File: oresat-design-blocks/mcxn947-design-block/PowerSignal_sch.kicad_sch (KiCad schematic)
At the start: 64 parts, among them J1 BKUP-BATT, J3 CAN, J4 TERM, J5 10pin ARM SWD, J6 FTDI-UART-6PIN, SW1 RESET, SW2 ISP(BOOT), U1 MCXN947VKLT, U2 TCAN330, U3 TPS62111RSA, Y1 24 MHz, Y2 32.768 KHz

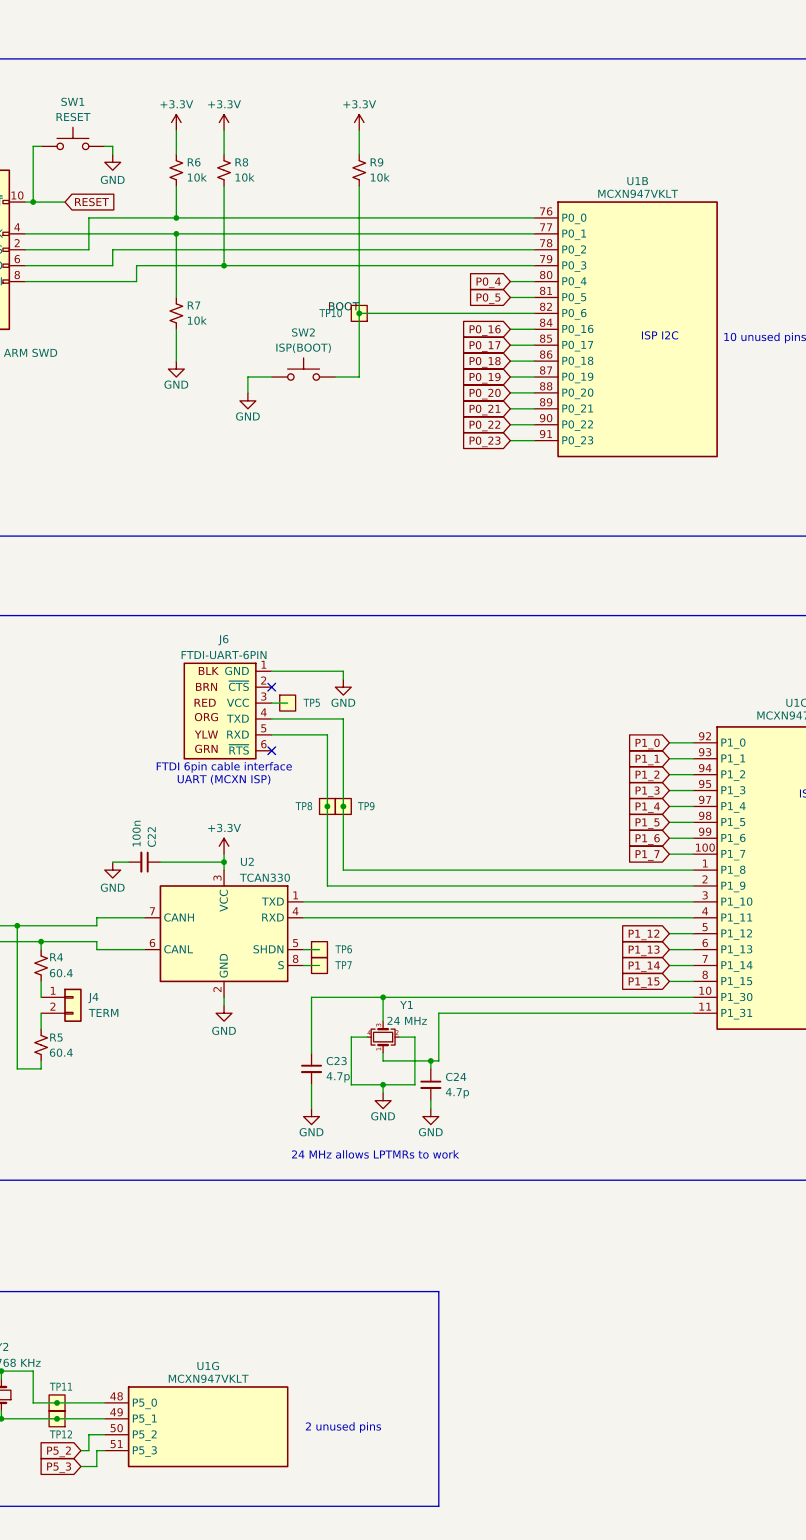
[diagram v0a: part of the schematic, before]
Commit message: finished initial layout and routing
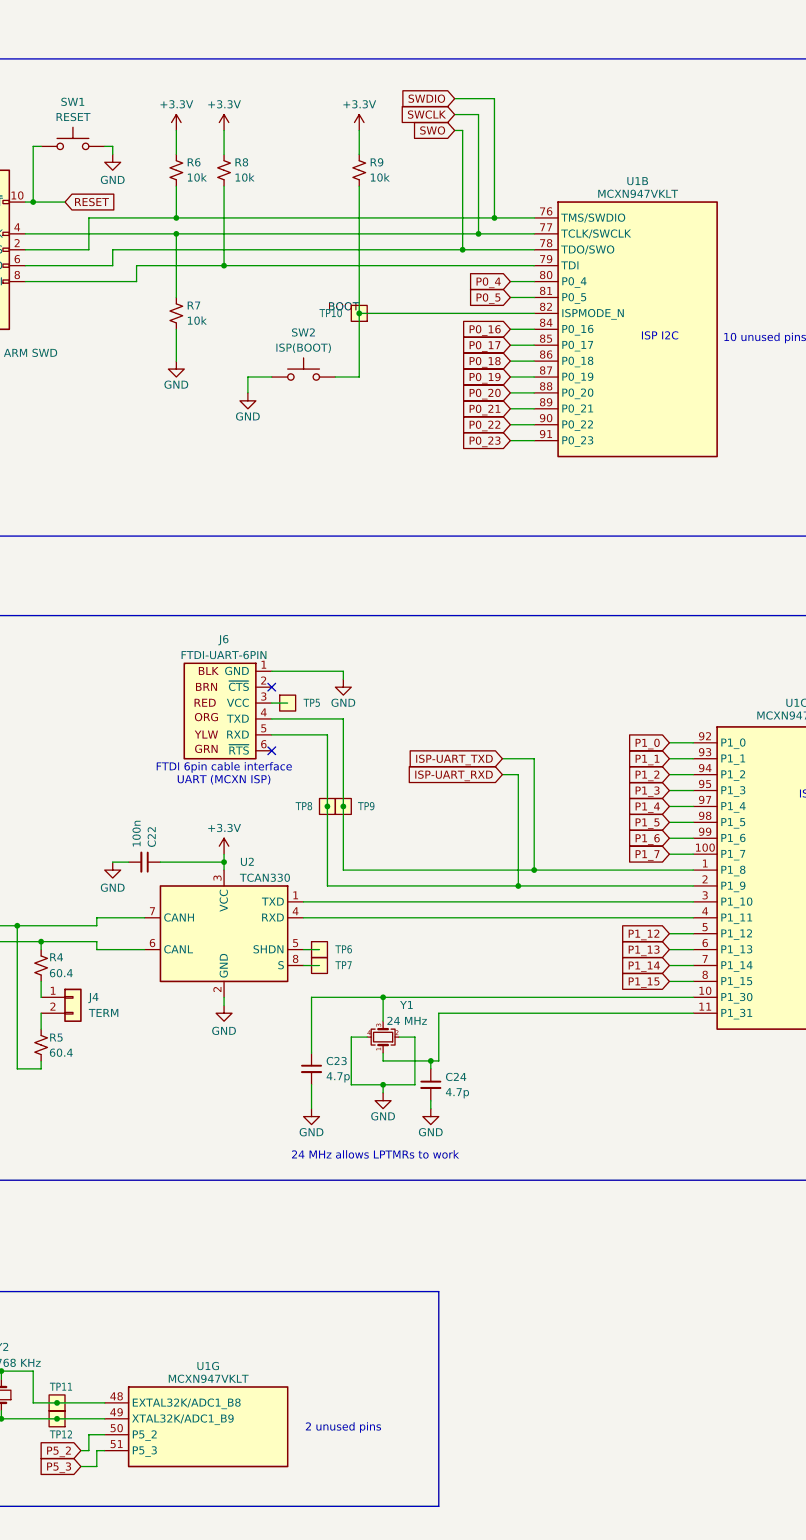
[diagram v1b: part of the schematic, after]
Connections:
- net ISP-UART_TXD: now reaches J6.4 (TXD), TP9.1, U1.1 (P1_8)
- net ISP-UART_RXD: now reaches J6.5 (RXD), TP8.1, U1.2 (P1_9)
- net SWDIO: now reaches J5.2 (SWDIO/TMS), R6.1, U1.76 (P0_0)
- net SWCLK: now reaches J5.4 (SWCLK/TCK), R7.2, U1.77 (P0_1)
- net SWO: now reaches J5.6 (SWO/TDO), U1.78 (P0_2)

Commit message: Some ERC checking and fixing, and then dep dive into oresat passive library. Sorry Anna. Go fix all the silkscreen.
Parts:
- C10, C11, C12, C13, C14, C15, C16, C2, C20, C22, C23, C24, C25, C26, C3, C4, C6, C7, C8, C9, R3, R4, R5, R6, R7, R8, R9: footprint oresat-passives:0603-B-NOSILK -> oresat-passives:0603-C-NOSILK
- C18, C5: footprint oresat-passives:0805-B-NOSILK -> oresat-passives:0603-C-NOSILK
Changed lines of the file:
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@@
 			)
 		)
-		(property "Footprint" "oresat-passives:0603-B-NOSILK"
+		(property "Footprint" "oresat-passives:0603-C-NOSILK"
 			(at 52.07 40.64 0)
 			(effects
@@
 			)
 		)
-		(property "Footprint" "oresat-passives:0603-B-NOSILK"
+		(property "Footprint" "oresat-passives:0603-C-NOSILK"
 			(at 254 43.18 0)
 			(effects
@@
 			)
 		)
-		(property "Footprint" "oresat-passives:0603-B-NOSILK"
+		(property "Footprint" "oresat-passives:0603-C-NOSILK"
 			(at 67.31 222.25 0)
 			(effects
@@
 			)
 		)
-		(property "Footprint" "oresat-passives:0603-B-NOSILK"
+		(property "Footprint" "oresat-passives:0603-C-NOSILK"
 			(at 80.01 228.6 0)
 			(effects
@@
 			)
 		)
-		(property "Footprint" "oresat-passives:0805-B-NOSILK"
+		(property "Footprint" "oresat-passives:0603-C-NOSILK"
 			(at 40.3352 86.36 0)
 			(effects
@@
 			)
 		)
-		(property "Footprint" "oresat-passives:0603-B-NOSILK"
+		(property "Footprint" "oresat-passives:0603-C-NOSILK"
 			(at 81.28 40.64 0)
 			(effects
@@
 			)
 		)
-		(property "Footprint" "oresat-passives:0603-B-NOSILK"
+		(property "Footprint" "oresat-passives:0603-C-NOSILK"
 			(at 232.41 170.18 0)
 			(effects
@@
 			)
 		)
-		(property "Footprint" "oresat-passives:0603-B-NOSILK"
+		(property "Footprint" "oresat-passives:0603-C-NOSILK"
 			(at 88.9 40.64 0)
 			(effects
@@
 			)
 		)
-		(property "Footprint" "oresat-passives:0603-B-NOSILK"
+		(property "Footprint" "oresat-passives:0603-C-NOSILK"
 			(at 143.51 144.78 0)
 			(effects
@@
 			)
 		)
-		(property "Footprint" "oresat-passives:0603-B-NOSILK"
+		(property "Footprint" "oresat-passives:0603-C-NOSILK"
 			(at 44.45 40.64 0)
 			(effects
@@
 			)
 		)
-		(property "Footprint" "oresat-passives:0603-B-NOSILK"
+		(property "Footprint" "oresat-passives:0603-C-NOSILK"
 			(at 111.76 40.64 0)
 			(effects
@@
 			)
 		)
-		(property "Footprint" "oresat-passives:0603-B-NOSILK"
+		(property "Footprint" "oresat-passives:0603-C-NOSILK"
 			(at 58.42 222.25 0)
 			(effects
@@
 			)
 		)
-		(property "Footprint" "oresat-passives:0603-B-NOSILK"
+		(property "Footprint" "oresat-passives:0603-C-NOSILK"
 			(at 294.64 189.23 0)
 			(effects
@@
 			)
 		)
-		(property "Footprint" "oresat-passives:0603-B-NOSILK"
+		(property "Footprint" "oresat-passives:0603-C-NOSILK"
 			(at 86.36 243.84 0)
 			(effects
@@
 			)
 		)
-		(property "Footprint" "oresat-passives:0603-B-NOSILK"
+		(property "Footprint" "oresat-passives:0603-C-NOSILK"
 			(at 50.8 208.28 0)
 			(effects
@@
 			)
 		)
-		(property "Footprint" "oresat-passives:0603-B-NOSILK"
+		(property "Footprint" "oresat-passives:0603-C-NOSILK"
 			(at 96.52 40.64 0)
 			(effects
@@
 			)
 		)
-		(property "Footprint" "oresat-passives:0603-B-NOSILK"
+		(property "Footprint" "oresat-passives:0603-C-NOSILK"
 			(at 73.66 40.64 0)
 			(effects
@@
 			)
 		)
-		(property "Footprint" "oresat-passives:0603-B-NOSILK"
+		(property "Footprint" "oresat-passives:0603-C-NOSILK"
 			(at 143.51 153.67 0)
 			(effects
@@
 			)
 		)
-		(property "Footprint" "oresat-passives:0603-B-NOSILK"
+		(property "Footprint" "oresat-passives:0603-C-NOSILK"
 			(at 275.59 186.69 0)
 			(effects
@@
 			)
 		)
-		(property "Footprint" "oresat-passives:0805-B-NOSILK"
+		(property "Footprint" "oresat-passives:0603-C-NOSILK"
 			(at 121.6152 87.63 0)
 			(effects
@@
 			)
 		)
-		(property "Footprint" "oresat-passives:0603-B-NOSILK"
+		(property "Footprint" "oresat-passives:0603-C-NOSILK"
 			(at 104.14 40.64 0)
 			(effects
@@
 			)
 		)
-		(property "Footprint" "oresat-passives:0603-B-NOSILK"
+		(property "Footprint" "oresat-passives:0603-C-NOSILK"
 			(at 283.21 43.18 0)
 			(effects
@@
 			)
 		)
-		(property "Footprint" "oresat-passives:0603-B-NOSILK"
+		(property "Footprint" "oresat-passives:0603-C-NOSILK"
 			(at 119.38 40.64 0)
 			(effects
@@
 			)
 		)
-		(property "Footprint" "oresat-passives:0603-B-NOSILK"
+		(property "Footprint" "oresat-passives:0603-C-NOSILK"
 			(at 261.62 43.18 0)
 			(effects
@@
 			)
 		)
-		(property "Footprint" "oresat-passives:0603-B-NOSILK"
+		(property "Footprint" "oresat-passives:0603-C-NOSILK"
 			(at 248.92 153.67 0)
 			(effects
@@
 			)
 		)
-		(property "Footprint" "oresat-passives:0603-B-NOSILK"
+		(property "Footprint" "oresat-passives:0603-C-NOSILK"
 			(at 218.44 242.57 0)
 			(effects
@@
 			)
 		)
-		(property "Footprint" "oresat-passives:0603-B-NOSILK"
+		(property "Footprint" "oresat-passives:0603-C-NOSILK"
 			(at 218.44 234.95 0)
 			(effects
@@
 			)
 		)
-		(property "Footprint" "oresat-passives:0603-B-NOSILK"
+		(property "Footprint" "oresat-passives:0603-C-NOSILK"
 			(at 254 66.04 0)
 			(effects
@@
 			)
 		)
-		(property "Footprint" "oresat-passives:0603-B-NOSILK"
+		(property "Footprint" "oresat-passives:0603-C-NOSILK"
 			(at 232.41 182.88 0)
 			(effects
